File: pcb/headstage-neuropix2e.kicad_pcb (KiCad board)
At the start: 4 copper layers, 60 x 60 mm, 64 parts, among them J1 X.FL-R-SMT-1(02), J2 FH35C-17S-0.3SHW(99), J3 FH35C-17S-0.3SHW(99), J4 SBH11-PBPC-D05-ST-BK, J5 TC2030, J6 050700622, U1 MIC5335-JGYMT, U2 NCP163AFCT180T2G, U3 DS90UB933TRTVTQ1, U4 STG3856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

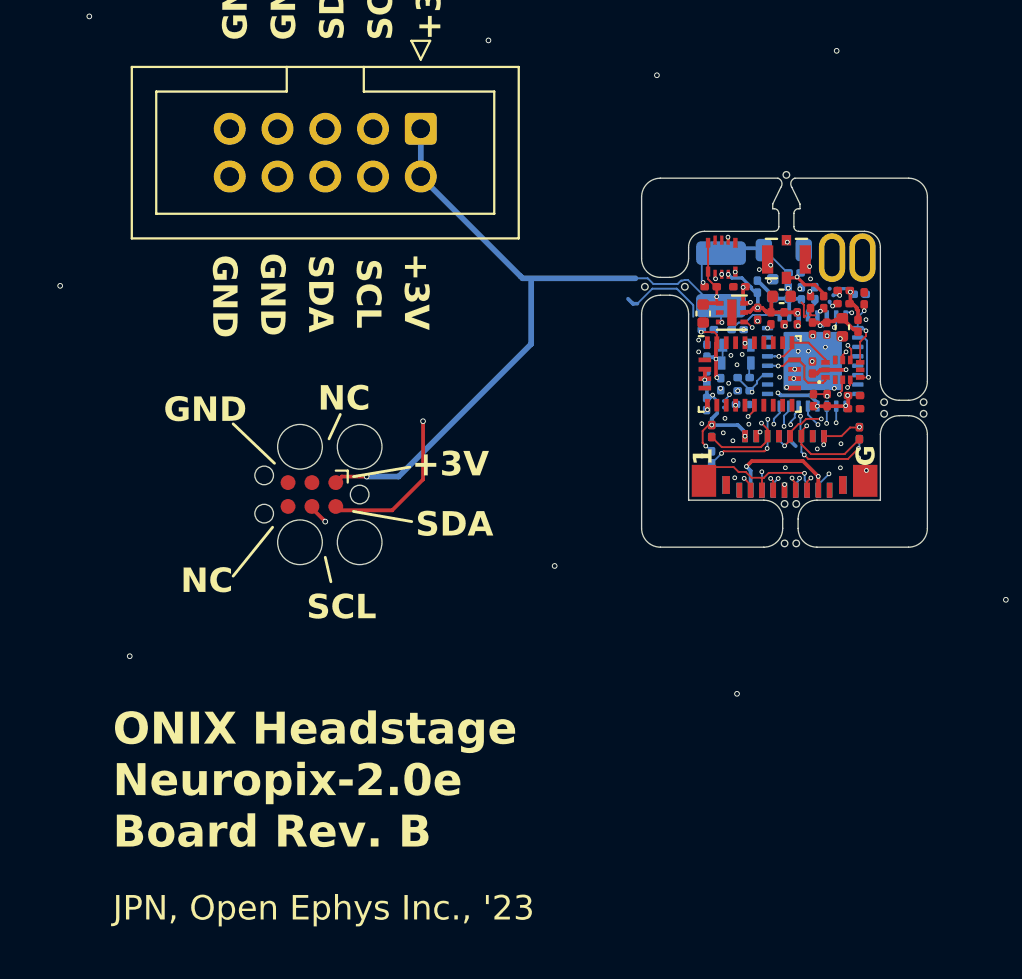
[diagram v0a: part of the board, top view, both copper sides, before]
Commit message: Rev. A of public version of headstage
- Being fabricated for testing
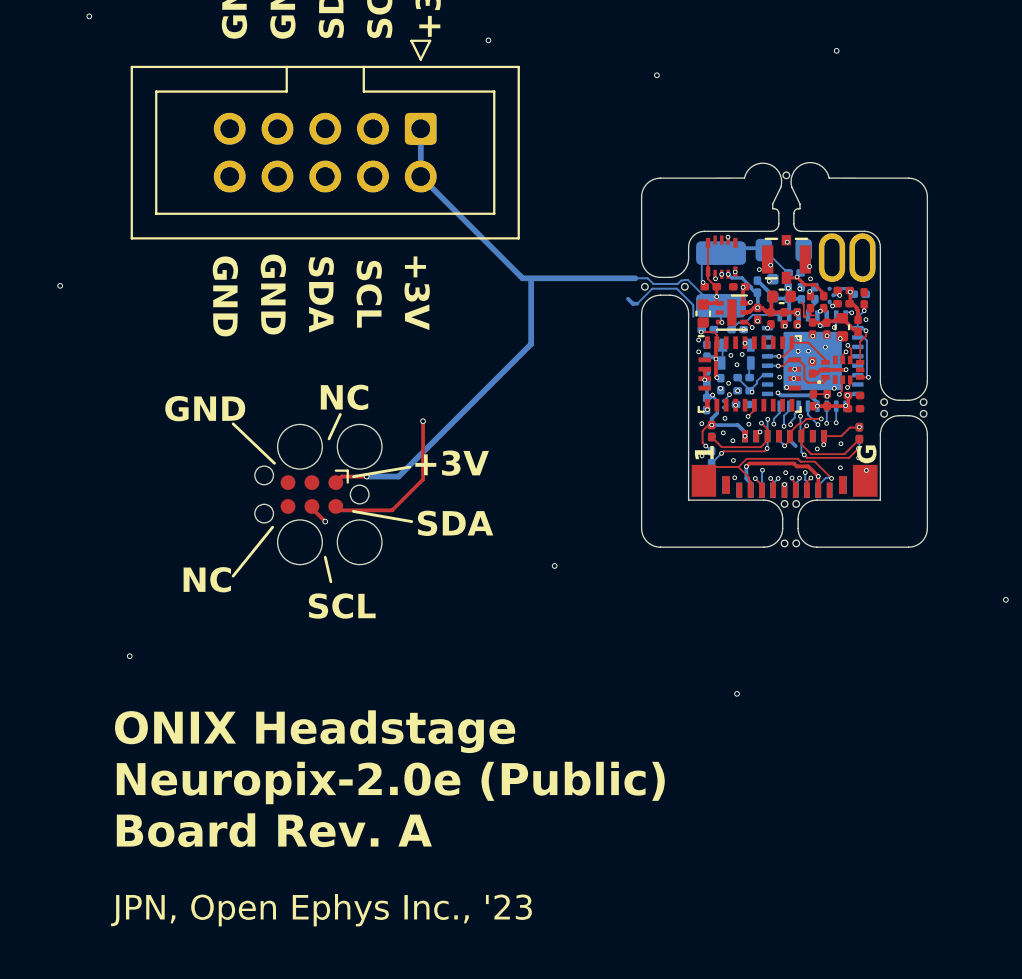
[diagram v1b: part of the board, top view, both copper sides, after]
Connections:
- J2 pad 13: /Neuropixels 2.0/NP_{TP1} -> /Neuropixels 2.0/NP_{TP0}
- J2 pad 15: /Neuropixels 2.0/NP_{TP0} -> /Neuropixels 2.0/NP_{TP1}
- J3 pad 13: /Neuropixels 2.0/NP_{TP1} -> /Neuropixels 2.0/NP_{TP0}
- J3 pad 15: /Neuropixels 2.0/NP_{TP0} -> /Neuropixels 2.0/NP_{TP1}
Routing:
- net /Neuropixels 2.0/NP_{TP1}: track 8.05 -> 11.1 mm
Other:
- outline, holes or cut-outs redrawn
- board text added: "ONIX Headstage Neuropix-2.0e (Public) Board Rev. A"
- board text removed: "ONIX Headstage Neuropix-2.0e Board Rev. B"
